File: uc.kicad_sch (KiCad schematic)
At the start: 1 part

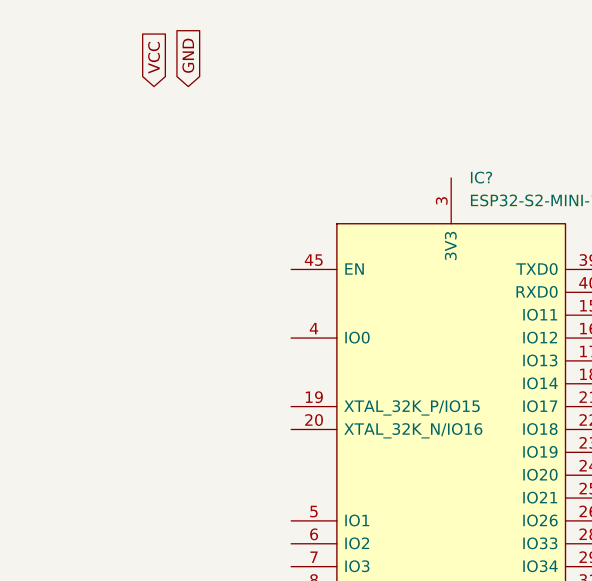
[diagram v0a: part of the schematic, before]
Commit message: now using correct VCC and GND symbols
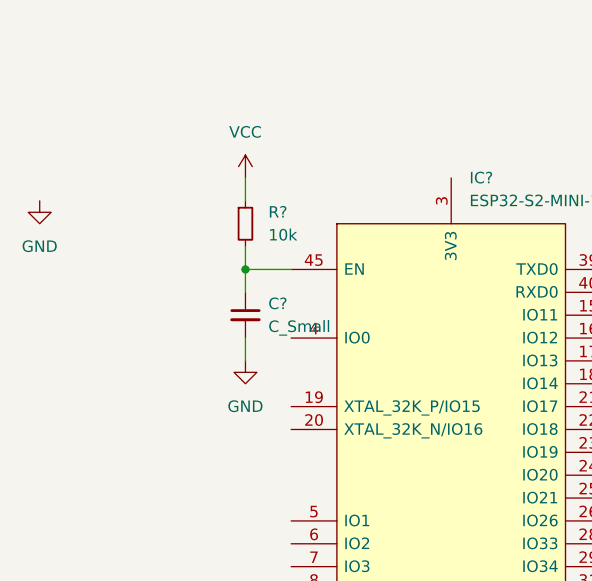
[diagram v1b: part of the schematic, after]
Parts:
- added C?: C_Small, symbol Device:C_Small
- added R?: 10k, symbol Device:R_Small
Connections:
- net GND: now also C?.2
- net VCC: now also R?.1
- net at IC?.45 (EN): now also C?.1, R?.2
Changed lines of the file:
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@@
 (kicad_sch (version 20211123) (generator eeschema)
   (paper "A4")
-  (global_label "VCC" (shape input) (at 48.26 31.75 90) (fields_autoplaced)
-    (effects (font (size 1.27 1.27)) (justify left))
-    (property "Intersheet References" "${INTERSHEET_REFS}" (id 0) (at 48.1806 25.7083 90)
-      (effects (font (size 1.27 1.27)) (justify left) hide)
-    )
-  )
-  (global_label "GND" (shape input) (at 52.07 31.75 90) (fields_autoplaced)
-    (effects (font (size 1.27 1.27)) (justify left))
-    (property "Intersheet References" "${INTERSHEET_REFS}" (id 0) (at 51.9906 25.4664 90)
-      (effects (font (size 1.27 1.27)) (justify left) hide)
-    )
+  (junction (at 58.42 52.07) (diameter 0) (color 0 0 0 0)
+  )
+  (wire (pts (xy 58.42 41.91) (xy 58.42 44.45))
+    (stroke (width 0) (type default) (color 0 0 0 0))
+  )
+  (wire (pts (xy 58.42 52.07) (xy 63.5 52.07))
+    (stroke (width 0) (type default) (color 0 0 0 0))
+  )
+  (wire (pts (xy 58.42 52.07) (xy 58.42 54.61))
+    (stroke (width 0) (type default) (color 0 0 0 0))
+  )
+  (wire (pts (xy 58.42 59.69) (xy 58.42 62.23))
+    (stroke (width 0) (type default) (color 0 0 0 0))
+  )
+  (wire (pts (xy 58.42 49.53) (xy 58.42 52.07))
+    (stroke (width 0) (type default) (color 0 0 0 0))
+  )
+  (symbol (lib_id "power:GND") (at 35.56 44.45 0) (unit 1)
+    (in_bom yes) (on_board yes) (fields_autoplaced)
+    (property "Reference" "#PWR?" (id 0) (at 35.56 50.8 0)
+      (effects (font (size 1.27 1.27)) hide)
+    )
+    (property "Value" "GND" (id 1) (at 35.56 49.53 0))
+    (property "Footprint" "" (id 2) (at 35.56 44.45 0)
+      (effects (font (size 1.27 1.27)) hide)
+    )
+    (property "Datasheet" "" (id 3) (at 35.56 44.45 0)
+      (effects (font (size 1.27 1.27)) hide)
+    )
+    (pin "1")
+  )
+  (symbol (lib_id "power:VCC") (at 58.42 41.91 0) (unit 1)
+    (in_bom yes) (on_board yes) (fields_autoplaced)
+    (property "Reference" "#PWR?" (id 0) (at 58.42 45.72 0)
+      (effects (font (size 1.27 1.27)) hide)
+    )
+    (property "Value" "VCC" (id 1) (at 58.42 36.83 0))
+    (property "Footprint" "" (id 2) (at 58.42 41.91 0)
+      (effects (font (size 1.27 1.27)) hide)
+    )
+    (property "Datasheet" "" (id 3) (at 58.42 41.91 0)
+      (effects (font (size 1.27 1.27)) hide)
+    )
+    (pin "1")
   )
   (symbol (lib_id "uc:ESP32-S2-MINI-1-N4R2") (at 81.28 80.01 0) (unit 1)
@@
     (pin "9")
   )
+  (symbol (lib_id "power:GND") (at 58.42 62.23 0) (unit 1)
+    (in_bom yes) (on_board yes) (fields_autoplaced)
+    (property "Reference" "#PWR?" (id 0) (at 58.42 68.58 0)
+      (effects (font (size 1.27 1.27)) hide)
+    )
+    (property "Value" "GND" (id 1) (at 58.42 67.31 0))
+    (property "Footprint" "" (id 2) (at 58.42 62.23 0)
+      (effects (font (size 1.27 1.27)) hide)
+    )
+    (property "Datasheet" "" (id 3) (at 58.42 62.23 0)
+      (effects (font (size 1.27 1.27)) hide)
+    )
+    (pin "1")
+  )
+  (symbol (lib_id "Device:R_Small") (at 58.42 46.99 0) (unit 1)
+    (in_bom yes) (on_board yes) (fields_autoplaced)
+    (property "Reference" "R?" (id 0) (at 60.96 45.7199 0)
+      (effects (font (size 1.27 1.27)) (justify left))
+    )
+    (property "Value" "10k" (id 1) (at 60.96 48.2599 0)
+      (effects (font (size 1.27 1.27)) (justify left))
+    )
+    (property "Footprint" "" (id 2) (at 58.42 46.99 0)
+      (effects (font (size 1.27 1.27)) hide)
+    )
+    (property "Datasheet" "~" (id 3) (at 58.42 46.99 0)
+      (effects (font (size 1.27 1.27)) hide)
+    )
+    (pin "1")
+    (pin "2")
+  )
+  (symbol (lib_id "Device:C_Small") (at 58.42 57.15 0) (unit 1)
+    (in_bom yes) (on_board yes) (fields_autoplaced)
+    (property "Reference" "C?" (id 0) (at 60.96 55.8862 0)
+      (effects (font (size 1.27 1.27)) (justify left))
+    )
+    (property "Value" "C_Small" (id 1) (at 60.96 58.4262 0)
+      (effects (font (size 1.27 1.27)) (justify left))
+    )
+    (property "Footprint" "" (id 2) (at 58.42 57.15 0)
+      (effects (font (size 1.27 1.27)) hide)
+    )
+    (property "Datasheet" "~" (id 3) (at 58.42 57.15 0)
+      (effects (font (size 1.27 1.27)) hide)
+    )
+    (pin "1")
+    (pin "2")
+  )
 )

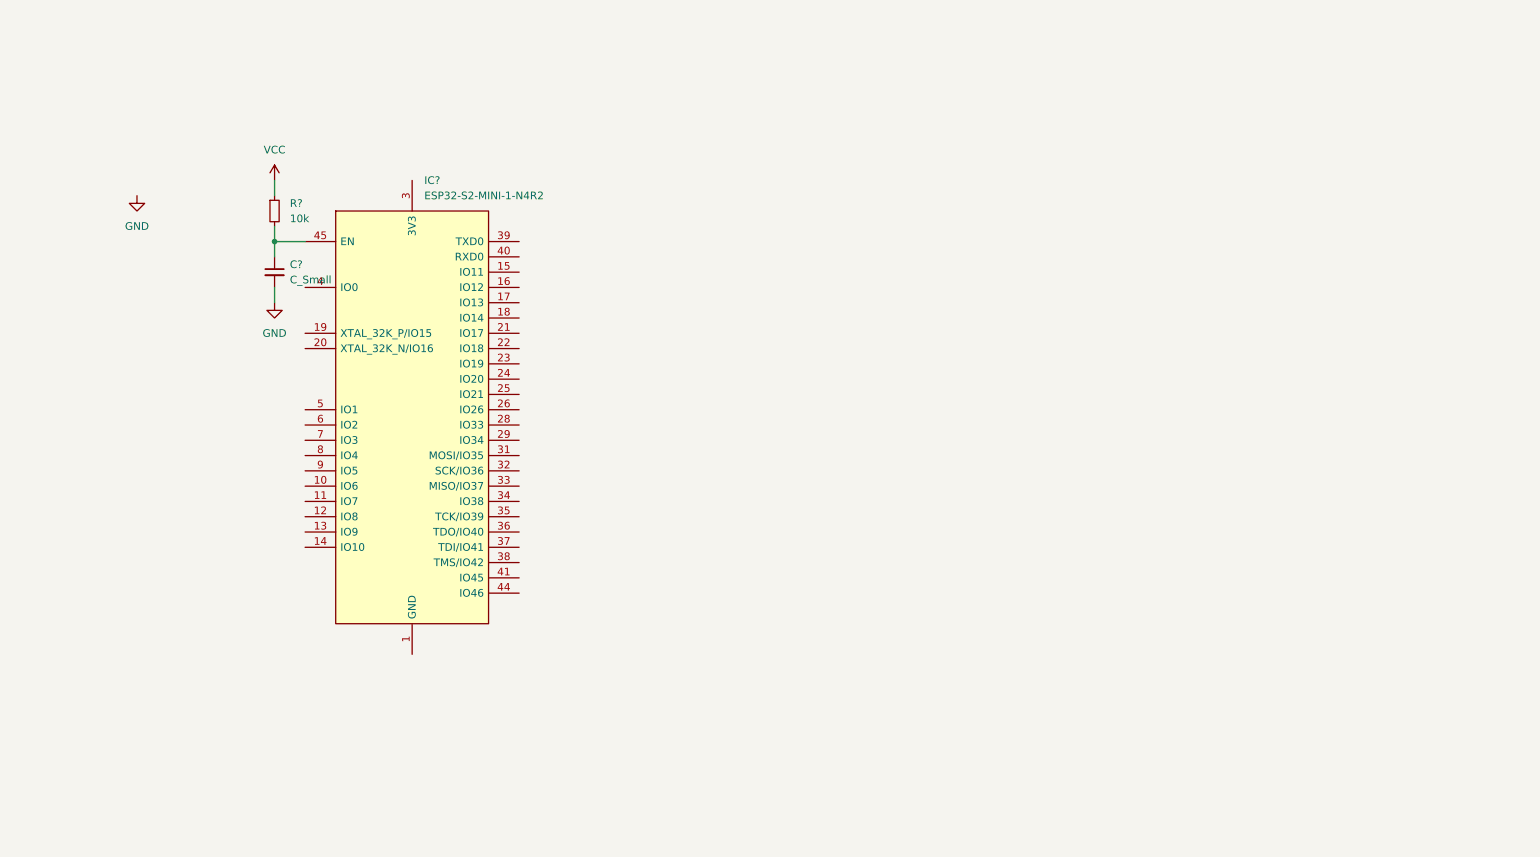
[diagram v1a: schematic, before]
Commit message: added esp32 schematic && updated supply symbols
Signed-off-by: Tobias Gent <gent.tobias@gmail.com>
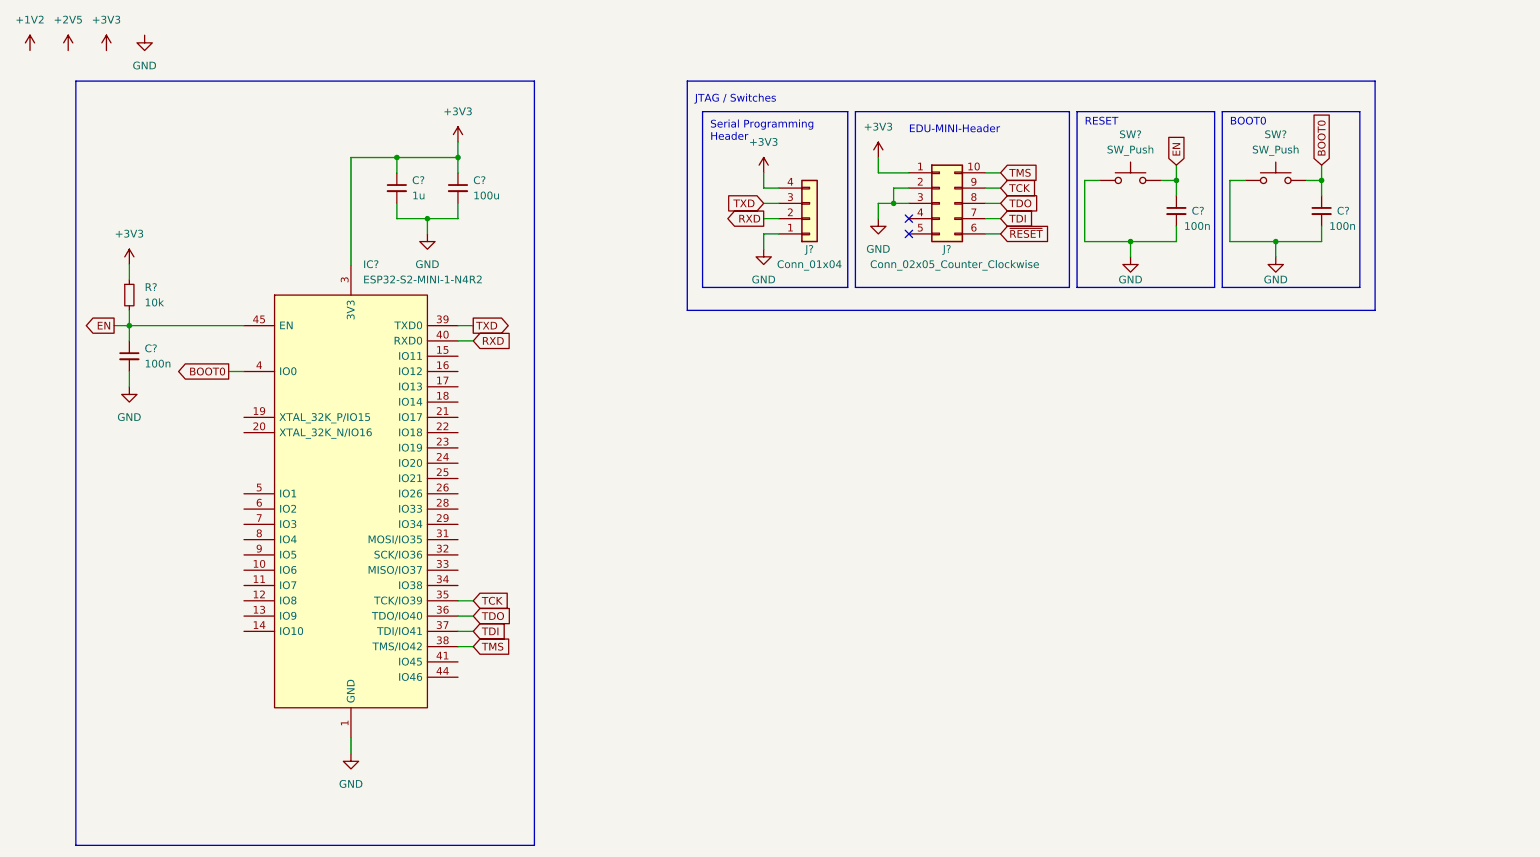
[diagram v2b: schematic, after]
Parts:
- added C? (x2): 100n, symbol Device:C_Small
- added C?: 1u, symbol Device:C_Small
- added C?: 100u, symbol Device:C_Small
- added J?: Conn_02x05_Counter_Clockwise, symbol Connector_Generic:Conn_02x05_Counter_Clockwise
- added J?: Conn_01x04, symbol Connector_Generic:Conn_01x04
- added SW? (x2): SW_Push, symbol Switch:SW_Push
- C?: value C_Small -> 100n
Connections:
- net VCC is gone; now on net +3V3: R?.1
- net GND: now also IC?.1 (GND), IC?.2 (GND_2), IC?.30 (GND_3), IC?.42 (GND_4), IC?.43 (GND_5), IC?.46 (GND_6), IC?.47 (GND_7), IC?.48 (GND_8), IC?.49 (GND_9), IC?.50 (GND_10), IC?.51 (GND_11), IC?.52 (GND_12), IC?.53 (GND_13), IC?.54 (GND_14), IC?.55 (GND_15), IC?.56 (GND_16), IC?.57 (GND_17), IC?.58 (GND_18), IC?.59 (GND_19), IC?.60 (GND_20), IC?.61 (GND_21), IC?.62 (GND_22), IC?.63 (GND_23), IC?.64 (GND_24), IC?.65 (GND_25), IC?.66 (GND_26), IC?.67 (GND_27), IC?.68 (GND_28), IC?.69 (GND_29), IC?.70 (GND_30), IC?.71 (GND_31), IC?.72 (GND_32), IC?.73 (GND_33), C?.2, C?.2, C?.2, C?.2, J?.1 (Pin_1), J?.2 (Pin_2), J?.3 (Pin_3), SW?.1, SW?.1
- net +3V3: now reaches IC?.3 (3V3)
- net +3V3: now also C?.1, C?.1, J?.1 (Pin_1), J?.4 (Pin_4)
- net TCK: now reaches IC?.35 (TCK/IO39)
- net TCK: now also J?.9 (Pin_9)
- net TDO: now reaches IC?.36 (TDO/IO40)
- net TDO: now also J?.8 (Pin_8)
- net TDI: now reaches IC?.37 (TDI/IO41)
- net TDI: now also J?.7 (Pin_7)
- net TMS: now reaches IC?.38 (TMS/IO42)
- net TMS: now also J?.10 (Pin_10)
- net TXD: now reaches IC?.39 (TXD0)
- net TXD: now also J?.3 (Pin_3)
- net BOOT0: now reaches IC?.4 (IO0)
- net BOOT0: now also C?.1, SW?.2
- net RXD: now reaches IC?.40 (RXD0)
- net RXD: now also J?.2 (Pin_2)
- net EN: now reaches C?.1, IC?.45 (EN), R?.2
- net EN: now also C?.1, SW?.2
- new net ~{RESET}: J?.6 (Pin_6)
- no-connect marks 0 -> 2
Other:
- note added: "BOOT0"
- note added: "EDU-MINI-Header"
- note added: "JTAG / Switches"
- note added: "RESET"
- note added: "Serial Programming Header"
- moved on the sheet: C?, IC?, R?

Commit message: added todo in uC
Signed-off-by: Tobias Gent <gent.tobias@gmail.com>
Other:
- note added: "TODO: - connection to FPGA - external FLASH? - external Crystal?"
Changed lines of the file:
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@@
+    (effects (font (size 1.27 1.27)) (justify left bottom))
+  )
+  (text "TODO:\n\n- connection to FPGA\n- external FLASH?\n- external Crystal?"
+    (at 130.81 90.17 0)
     (effects (font (size 1.27 1.27)) (justify left bottom))
   )

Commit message: updated TODO
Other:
- note added: "TODO: - connection to FPGA - external FLASH? - external Crystal? - EDU-MINI JTAG possible?"
- note removed: "TODO: - connection to FPGA - external FLASH? - external Crystal?"
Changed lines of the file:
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@@
     (effects (font (size 1.27 1.27)) (justify left bottom))
   )
-  (text "TODO:\n\n- connection to FPGA\n- external FLASH?\n- external Crystal?"
+  (text "TODO:\n\n- connection to FPGA\n- external FLASH?\n- external Crystal?\n- EDU-MINI JTAG possible?"
     (at 130.81 90.17 0)
     (effects (font (size 1.27 1.27)) (justify left bottom))

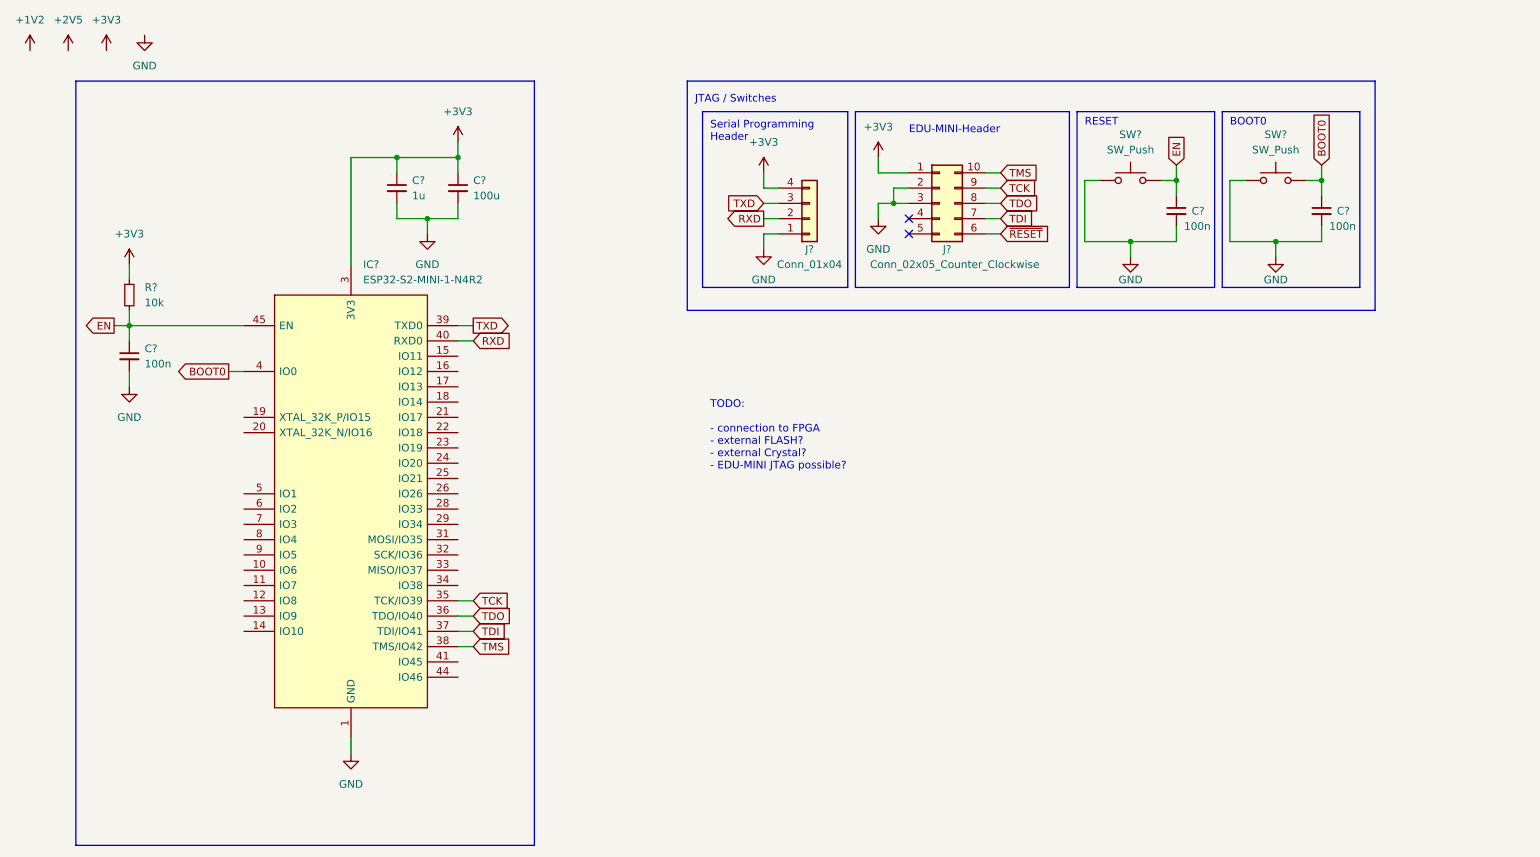
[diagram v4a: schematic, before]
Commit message: removed JTAG, added bootstrap circuit
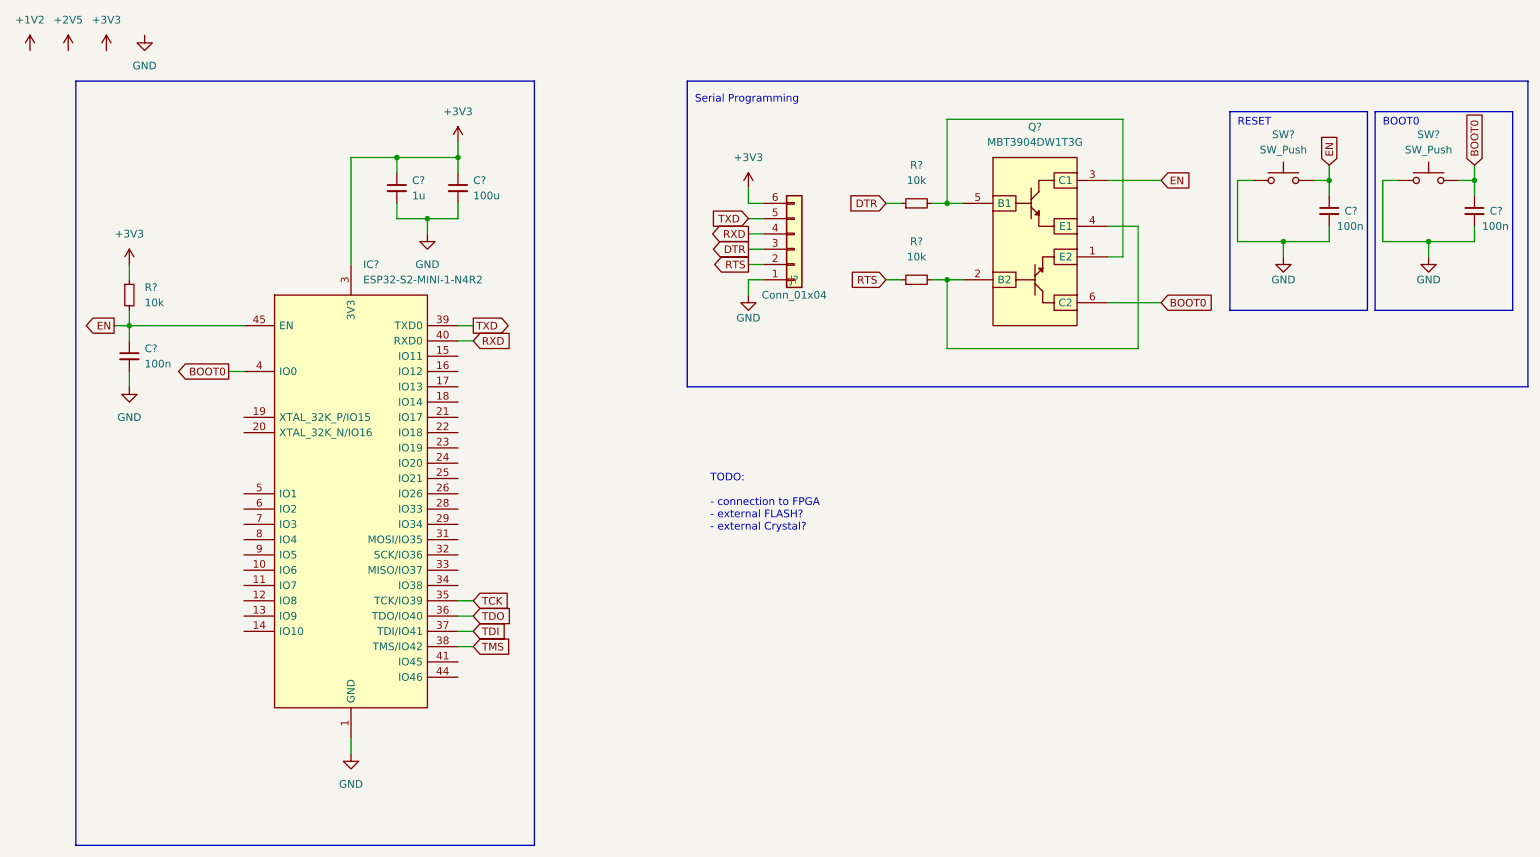
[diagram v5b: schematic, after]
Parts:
- removed J?: Conn_02x05_Counter_Clockwise, symbol Connector_Generic:Conn_02x05_Counter_Clockwise
- removed J?: Conn_01x04, symbol Connector_Generic:Conn_01x04
- added J?: Conn_01x04, symbol Connector_Generic:Conn_01x06
- added Q?: MBT3904DW1T3G, SOT65P210X110-6N, symbol uc:MBT3904DW1T3G
- added R? (x2): 10k, symbol Device:R_Small
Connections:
- net +3V3: now also J?.6 (Pin_6)
- net BOOT0: now also Q?.6 (C2)
- net EN: now also Q?.3 (C1)
- net GND: now also J?.1 (Pin_1)
- net RXD: now also J?.4 (Pin_4)
- net TXD: now also J?.5 (Pin_5)
- new net: Q?.2 (B2), Q?.4 (E1), R?.2
- new net: Q?.1 (E2), Q?.5 (B1), R?.2
- new net DTR: J?.3 (Pin_3), R?.1
- new net RTS: J?.2 (Pin_2), R?.1
- no-connect marks 2 -> 0
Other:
- note added: "Serial Programming"
- note added: "TODO: - connection to FPGA - external FLASH? - external Crystal?"
- note removed: "EDU-MINI-Header"
- note removed: "JTAG / Switches"
- note removed: "Serial Programming Header"
- note removed: "TODO: - connection to FPGA - external FLASH? - external Crystal? - EDU-MINI JTAG possible?"
- moved on the sheet: C?, SW?
